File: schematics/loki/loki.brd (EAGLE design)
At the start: 100 x 49 mm, 56 parts, among them IC2 LM358D, Q1 MOSFET-PCHANNELSMD, U1 USD SOCKET, U2 CY8C5XXX-100PIN, Y1 XRCGB_XTAL

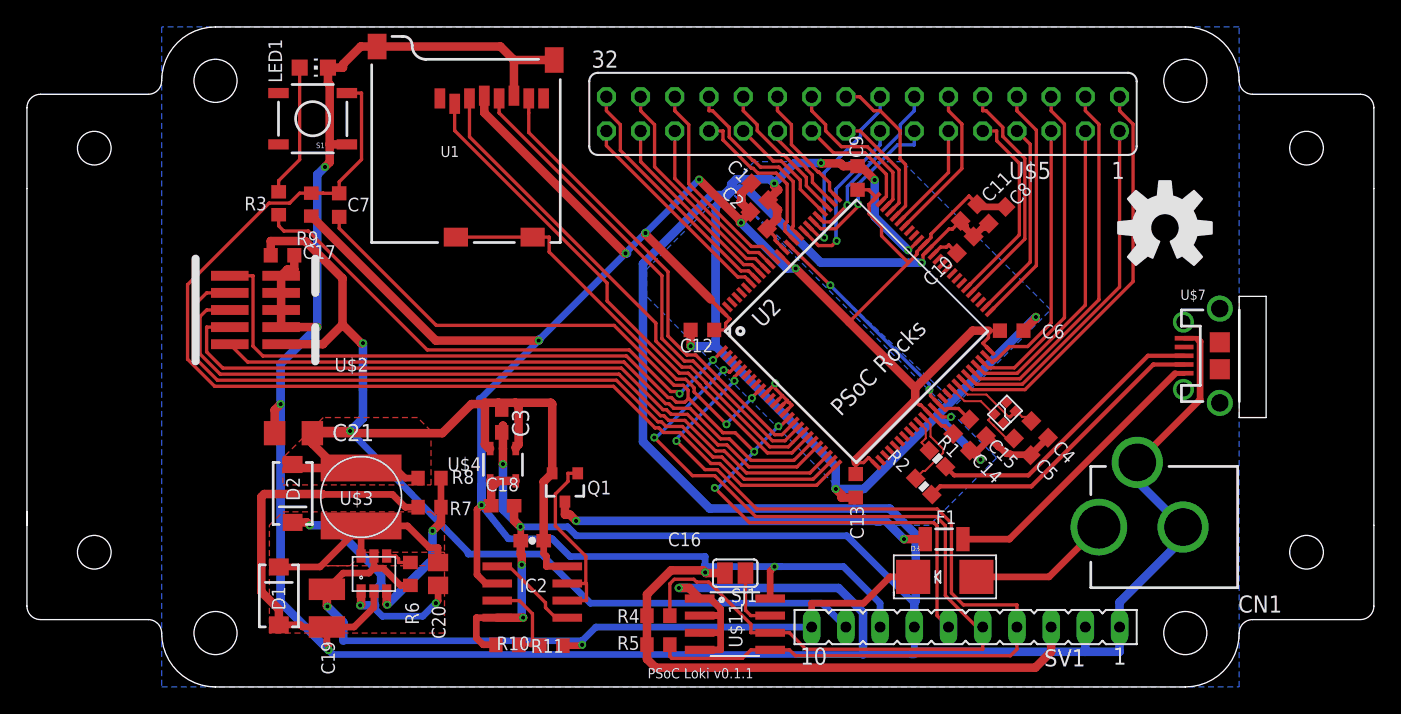
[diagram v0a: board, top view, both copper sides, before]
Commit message: Misc layout improvements to Loki; updated to v0.2.
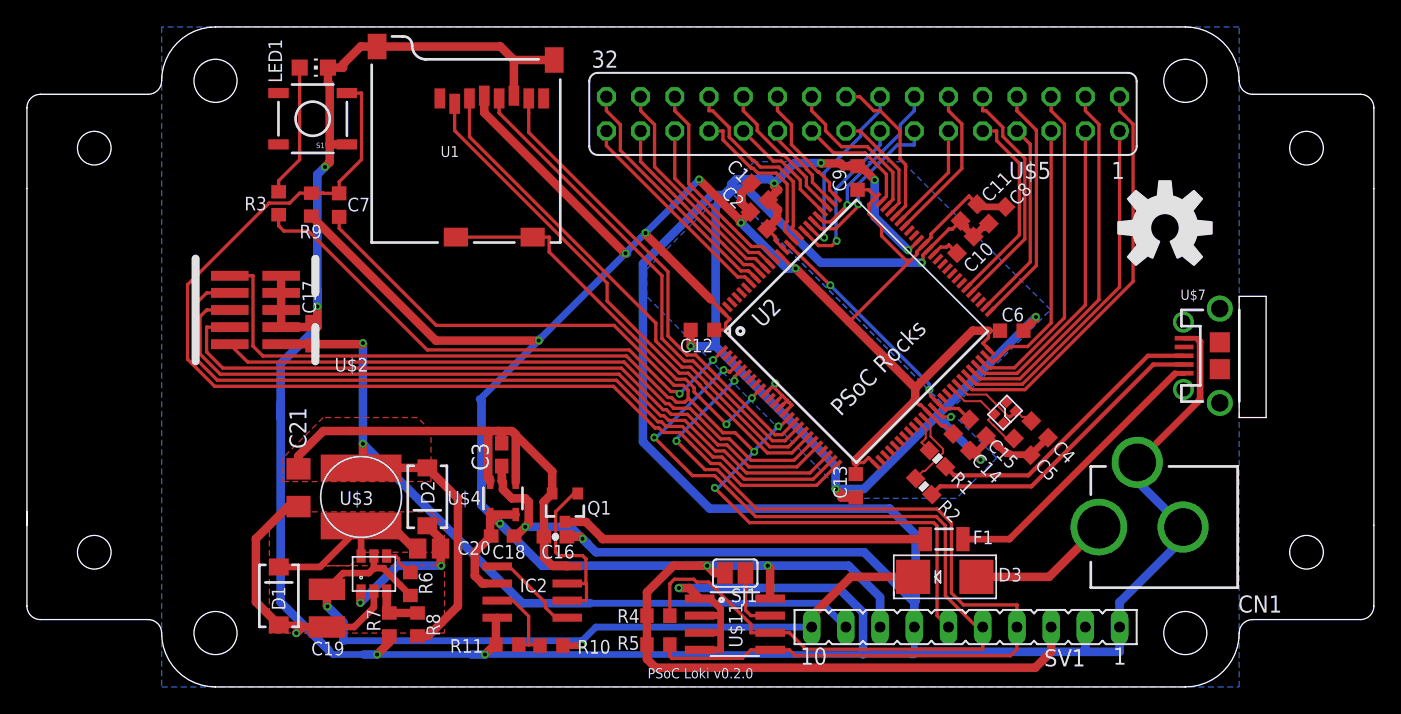
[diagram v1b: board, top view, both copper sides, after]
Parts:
- moved R8 10.9 mm to (19.0, 4.64), turned to 270 degrees
- moved D2 10.0 mm to (19.7, 14.1)
- moved R7 9.20 mm to (16.9, 4.64), turned to 90 degrees
- moved C17 6.23 mm to (11.2, 26.2), turned to 90 degrees
- moved C21 4.07 mm to (10.2, 14.8), turned to 270 degrees
- moved C3 2.50 mm to (25.2, 17.2)
- moved U$4 2.50 mm to (25.3, 14.0)
- moved C18 2.25 mm to (25.3, 11.2)
- moved C20 2.00 mm to (19.9, 10.3), turned to 180 degrees
- moved C16 1.74 mm to (29.2, 11.1), turned to 0 degrees
- moved Q1 1.50 mm to (29.9, 13.4)
- moved R6 0.75 mm to (18.5, 7.64)
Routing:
- net GND: track 345.2 -> 329.2 mm, vias 9 -> 8
- net FB: track 12.1 -> 3.80 mm, vias 2 -> 0
- net BOOST: track 19.7 -> 11.4 mm, vias 3 -> 2
- net +5V: track 124.6 -> 121.8 mm
- net INDIN: track 17.1 -> 14.5 mm
- net USBVCC: track 28.5 -> 27.3 mm, vias 2 -> 0
- net N$13: track 14.3 -> 13.6 mm
- net +3V3: track 253.9 -> 253.3 mm
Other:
- board text added: "PSoC Loki v0.2.0"
- board text removed: "PSoC Loki v0.1.1"

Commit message: Added missing board file from previous commit.
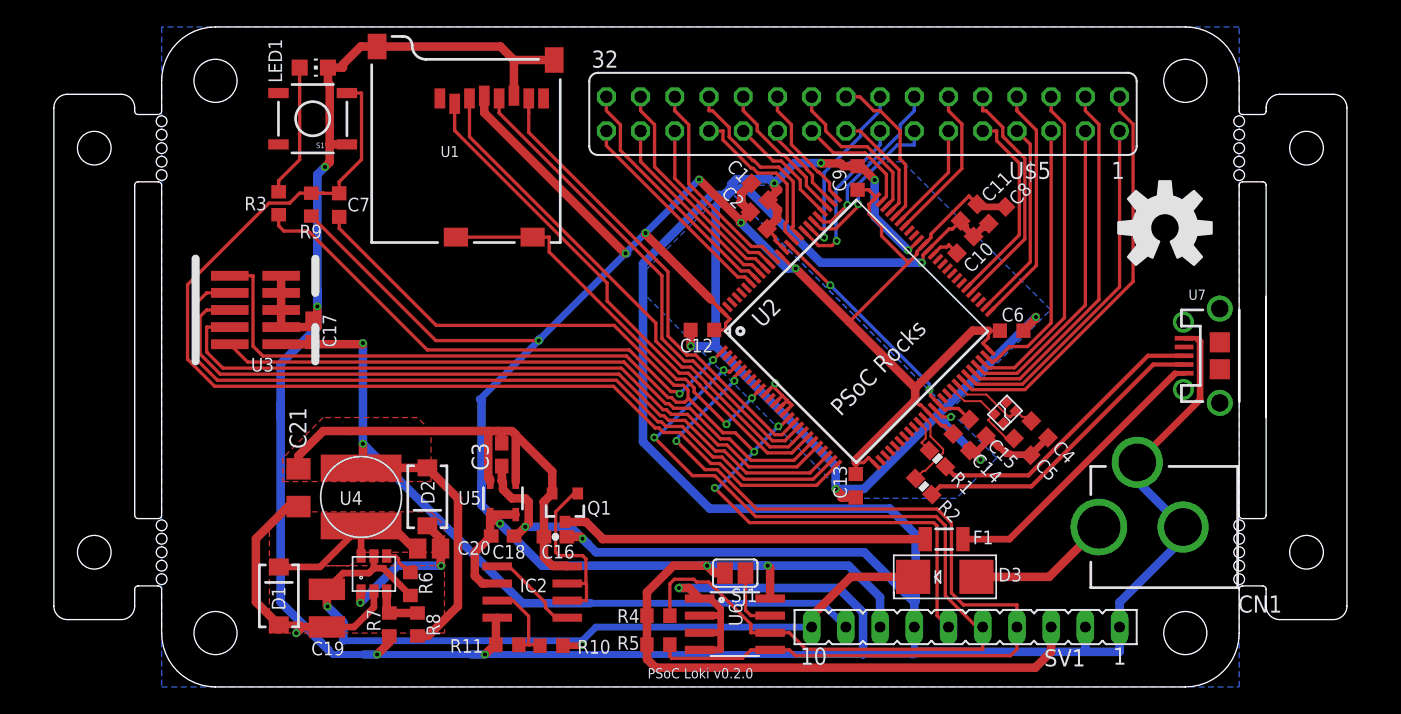
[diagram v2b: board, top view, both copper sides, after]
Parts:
- U2: value CY8C5XXX-100PIN -> CY8C5XXX
- moved C17 0.25 mm to (11.2, 26.5)
- renumbered U$11 to U6, U$2 to U3, U$3 to U4, U$4 to U5, U$7 to U7
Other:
- board size 100 x 49 mm -> 96 x 49 mm

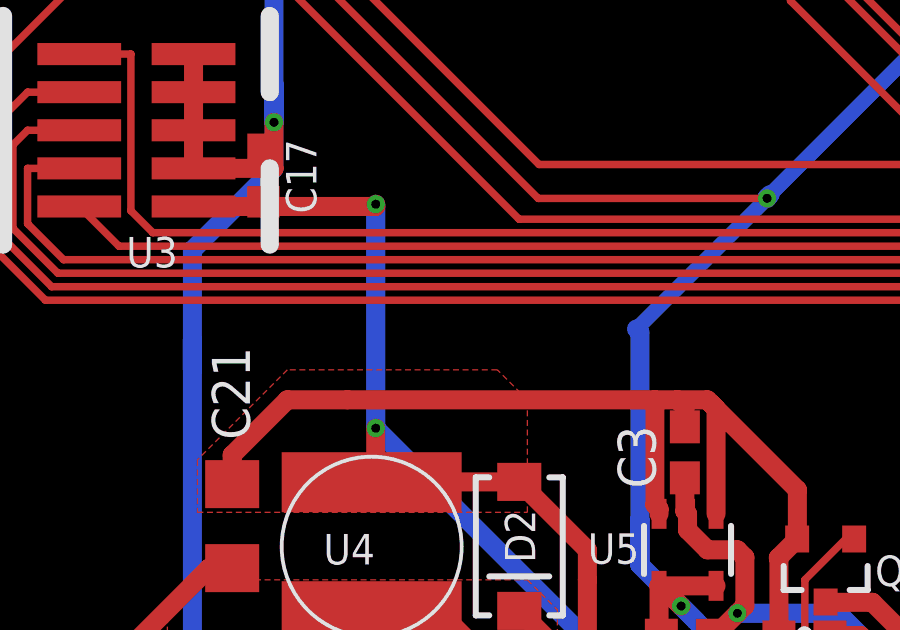
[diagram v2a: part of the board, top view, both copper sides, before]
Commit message: Fixed both Loki and the programmer to use 3.3v for power on programming headers.
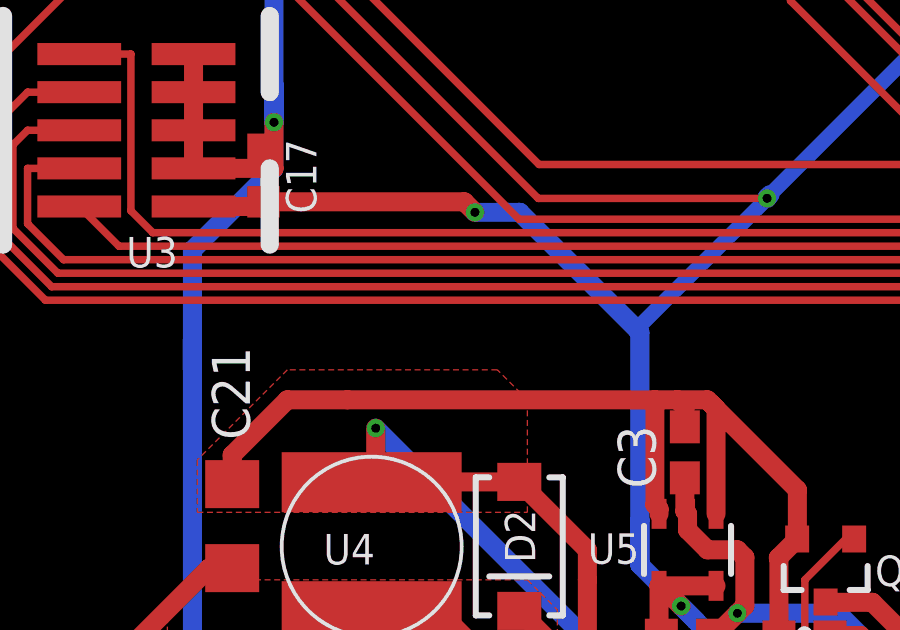
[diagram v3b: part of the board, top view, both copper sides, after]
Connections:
- net +3V3: now also C17.1, U3.P$1
- net +5V: no longer C17.1, U3.P$1
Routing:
- net +3V3: track 253.3 -> 269.9 mm, vias 9 -> 10
- net +5V: track 121.8 -> 108.1 mm, vias 2 -> 1
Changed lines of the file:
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@@
 <param name="mlMinStopFrame" value="2mil"/>
 <param name="mlMaxStopFrame" value="2mil"/>
-<param name="mlMinCreamFrame" value="4mil"/>
-<param name="mlMaxCreamFrame" value="4mil"/>
+<param name="mlMinCreamFrame" value="0mil"/>
+<param name="mlMaxCreamFrame" value="0mil"/>
 <param name="mlViaStopLimit" value="100mil"/>
 <param name="srRoundness" value="0"/>
@@
 <contactref element="U5" pad="3"/>
 <contactref element="SV1" pad="9"/>
-<contactref element="U3" pad="P$1"/>
-<contactref element="C17" pad="1"/>
-<via x="14.9456" y="25.52" extent="1-16" drill="0.3" diameter="0.6048"/>
 <wire x1="16.3171" y1="16.255" x2="17.3369" y2="16.255" width="0.5" layer="1"/>
 <wire x1="49.0291" y1="6.2159" x2="50.8" y2="4.445" width="0.5" layer="16"/>
@@
 <wire x1="10.16" y1="17.16" x2="12" y2="19" width="0.635" layer="1"/>
 <wire x1="12" y1="19" x2="14" y2="19" width="0.635" layer="1"/>
-<wire x1="14.9456" y1="25.52" x2="14.9456" y2="18.0544" width="0.635" layer="16"/>
 <via x="14.9456" y="18.0544" extent="1-16" drill="0.3"/>
 <wire x1="14.9456" y1="18.0544" x2="14.9456" y2="16.3906" width="0.635" layer="1"/>
@@
 <wire x1="26.2892" y1="15.1986" x2="26.2892" y2="18.7108" width="0.635" layer="1"/>
 <wire x1="26.2892" y1="18.7108" x2="26.125" y2="18.875" width="0.635" layer="1"/>
-<wire x1="8.872" y1="25.4451" x2="11.2031" y2="25.4451" width="0.635" layer="1"/>
-<wire x1="11.2031" y1="25.4451" x2="11.2031" y2="25.6006" width="0.635" layer="1"/>
-<wire x1="11.2031" y1="25.4451" x2="14.9456" y2="25.4451" width="0.635" layer="1"/>
-<wire x1="14.9456" y1="25.4451" x2="14.9456" y2="25.52" width="0.635" layer="1"/>
 </signal>
 <signal name="+3V3">
@@
 <wire x1="27.9912" y1="25.7137" x2="20.3607" y2="25.7137" width="0.25" layer="1"/>
 <wire x1="20.3607" y1="25.7137" x2="11.1164" y2="34.958" width="0.25" layer="1"/>
+<contactref element="U3" pad="P$1"/>
+<contactref element="C17" pad="1"/>
+<wire x1="8.872" y1="25.4451" x2="11.2031" y2="25.4451" width="0.635" layer="1"/>
+<wire x1="11.2031" y1="25.4451" x2="11.2031" y2="25.6006" width="0.635" layer="1"/>
+<wire x1="11.2031" y1="25.6006" x2="17.8994" y2="25.6006" width="0.635" layer="1"/>
+<wire x1="17.8994" y1="25.6006" x2="18.25" y2="25.25" width="0.635" layer="1"/>
+<via x="18.25" y="25.25" extent="1-16" drill="0.3"/>
+<wire x1="18.25" y1="25.25" x2="19.75" y2="25.25" width="0.635" layer="16"/>
+<wire x1="19.75" y1="25.25" x2="23.63875" y2="21.36125" width="0.635" layer="16"/>
 </signal>
 <signal name="SWDIO">

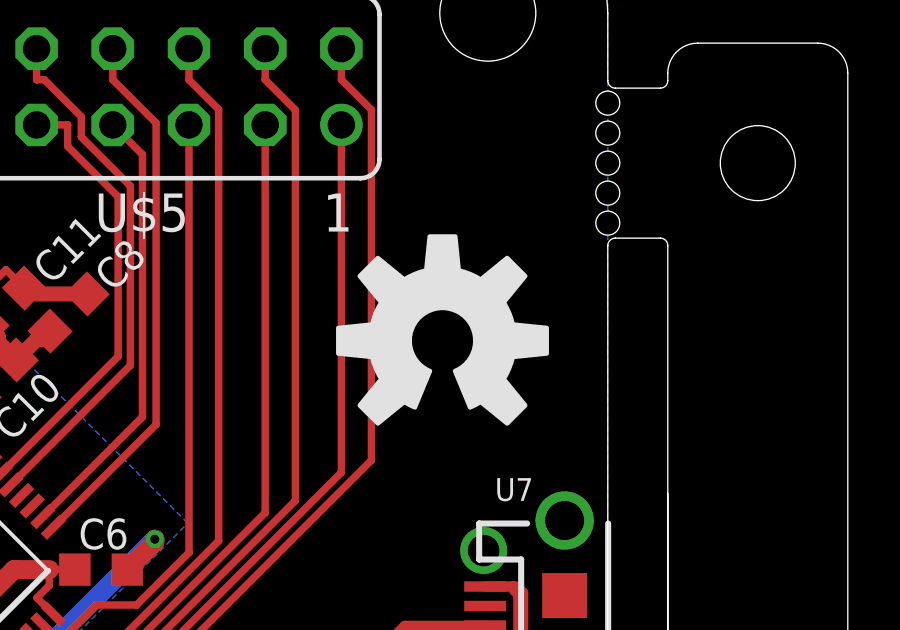
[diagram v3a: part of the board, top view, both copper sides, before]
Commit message: Implemented bootloader host.
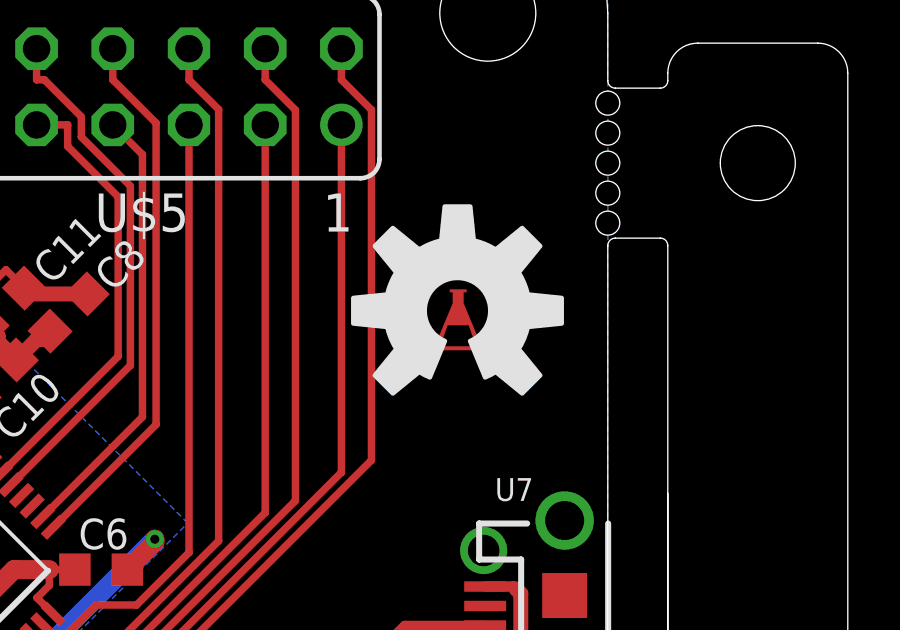
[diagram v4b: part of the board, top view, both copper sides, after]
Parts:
- added U$1: (no value), nickparts:ARACHNID_LABS_LOGO_SM
- moved U$12 1.12 mm to (75.0, 35.1)
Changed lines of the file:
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@@
 <layer number="31" name="tCream" color="7" fill="4" visible="no" active="yes"/>
 <layer number="32" name="bCream" color="7" fill="5" visible="no" active="yes"/>
-<layer number="33" name="tFinish" color="6" fill="3" visible="no" active="yes"/>
-<layer number="34" name="bFinish" color="6" fill="6" visible="no" active="yes"/>
+<layer number="33" name="tFinish" color="6" fill="3" visible="yes" active="yes"/>
+<layer number="34" name="bFinish" color="6" fill="6" visible="yes" active="yes"/>
 <layer number="35" name="tGlue" color="7" fill="4" visible="yes" active="yes"/>
 <layer number="36" name="bGlue" color="7" fill="5" visible="yes" active="yes"/>
@@
 <attribute name="NAME" x="35.4844" y="3.7742" size="1.016" layer="25" rot="R180"/>
 </element>
-<element name="U$12" library="SparkFun-Aesthetics" package="OSHW-LOGO-L" value="" x="74.49" y="34.08"/>
+<element name="U$12" library="SparkFun-Aesthetics" package="OSHW-LOGO-L" value="" x="74.99" y="35.08"/>
 <element name="U$6" library="loki" package="LOKI_LOGO" value="" x="32.7764" y="25.0208"/>
 <element name="D3" library="adafruit" package="SMADIODE" value="" x="58.1435" y="8.1712" smashed="yes">
@@
 <attribute name="NAME" x="23.012" y="18.139" size="1.27" layer="25" rot="R270"/>
 </element>
+<element name="U$1" library="nickparts" package="ARACHNID_LABS_LOGO_SM" value="" x="71" y="30"/>
 </elements>
 <signals>
@@
 </signal>
 </signals>
-<errors>
-</errors>
 </board>
 </drawing>
